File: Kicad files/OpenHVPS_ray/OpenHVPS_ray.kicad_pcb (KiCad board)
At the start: 2 copper layers, 45.8 x 20.6 mm, 69 parts, among them J1 Conn_01x03_Male, J2 Conn_01x03_Male, Q1 FQT7N10, Q2 BC846A, Q3 MMDT3906, U1 MAX6008AEUR+T, U2 74HC14, U3 MAX4162, U4 CD14538BM

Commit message: Added rays version
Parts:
- removed J1: Conn_01x03_Male, Connector_PinHeader_2.54mm:PinHeader_1x03_P2.54mm_Vertical
- removed JP1: 7317, Jumper:SolderJumper-2_P1.3mm_Open_RoundedPad1.0x1.5mm
- removed R2: 10M, Resistor_SMD:R_1206_3216Metric
- added REF**: PinHeader_1x01_P2.54mm_Vertical, Connector_PinHeader_2.54mm:PinHeader_1x01_P2.54mm_Vertical, F.Cu at (164.6, 75.7)
- added REF**: PinHeader_1x01_P2.54mm_Vertical, Connector_PinHeader_2.54mm:PinHeader_1x01_P2.54mm_Vertical, F.Cu at (125.2, 75.7)
- added REF**: PinHeader_1x01_P2.54mm_Vertical, Connector_PinHeader_2.54mm:PinHeader_1x01_P2.54mm_Vertical, F.Cu at (164.3, 59.4)
- added REF**: PinHeader_1x01_P2.54mm_Vertical, Connector_PinHeader_2.54mm:PinHeader_1x01_P2.54mm_Vertical, F.Cu at (125.2, 59.7)
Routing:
- net GND: track 118.9 -> 125.2 mm, vias 14 -> 13
- net Net-(H2-Pad1): track 7.99 -> 4.16 mm
- net +3V3: track 65.5 -> 63.2 mm
- net Net-(C21-Pad2): track 8.04 -> 5.94 mm
- net Net-(D2-Pad2): track 34.6 -> 32.5 mm
- net Net-(JP1-Pad1): track 1.70 -> 0.00 mm
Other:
- board size 45.8 x 20.6 mm -> 43.4 x 20.6 mm
- board text added: "SafePulse V0.9 (ray)"
- board text removed: "SafePulse V0.9"

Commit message: Added Ray version
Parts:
- removed the REF** at (164.6, 75.7)
- removed the REF** at (125.2, 75.7)
- removed the REF** at (125.2, 59.7)
- added ?: LOGO, Symbol:QR_code_SafePulse, F.Cu at (157.2, 66.3)
- added H2: Anode, TestPoint:TestPoint_Loop_D2.50mm_Drill1.85mm, F.Cu at (164.3, 72.4)
- added REF**: PinHeader_1x01_P2.54mm_Vertical, Connector_PinHeader_2.54mm:PinHeader_1x01_P2.54mm_Vertical, F.Cu at (164.3, 62.2)
- H1, H2: footprint TestPoint:TestPoint_Loop_D3.80mm_Drill2.0mm -> TestPoint:TestPoint_Loop_D2.50mm_Drill1.0mm
- moved H2 1.95 mm to (164.3, 68.8)
- moved R1 1.04 mm to (164.1, 65.5), turned to 0 degrees
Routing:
- net GND: track 125.2 -> 121.0 mm
- net Net-(H2-Pad1): track 4.16 -> 8.16 mm
- net Net-(C21-Pad2): track 5.94 -> 7.63 mm
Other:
- board size 43.4 x 20.6 mm -> 40.6 x 20.8 mm

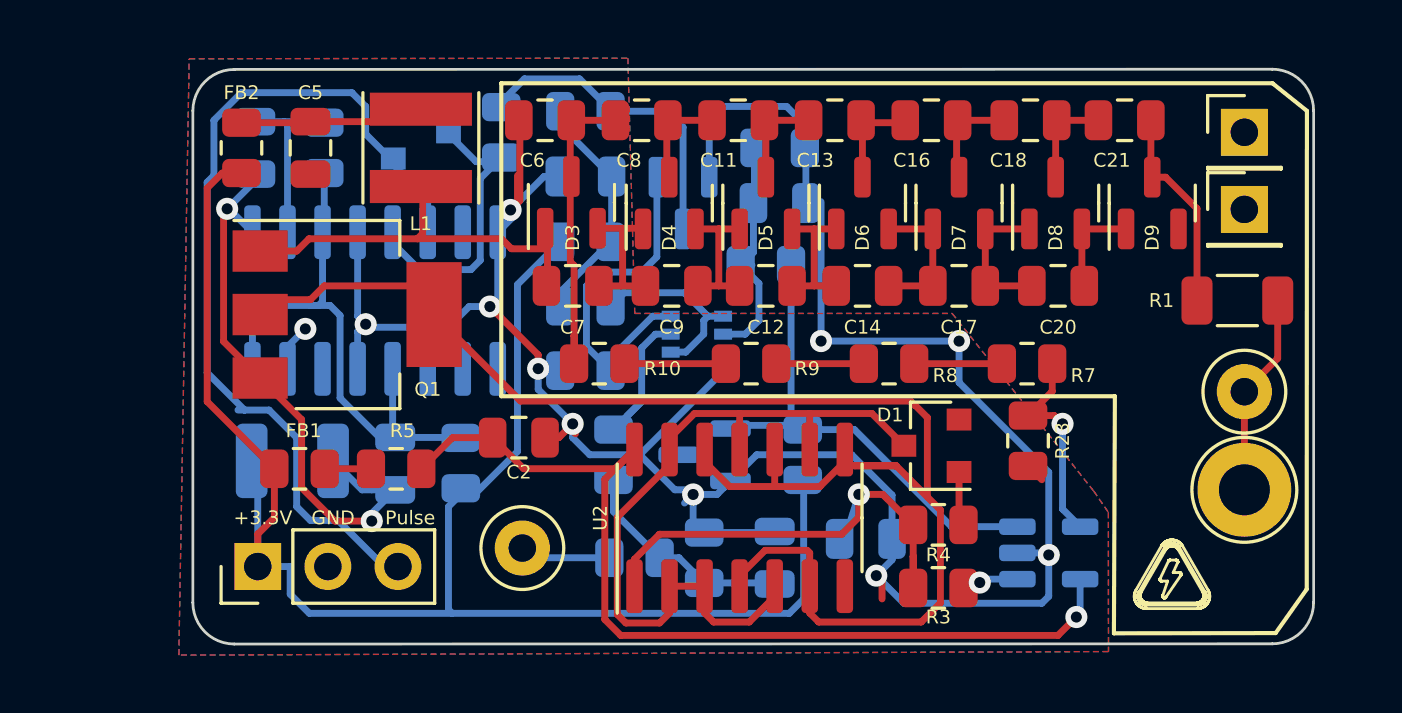
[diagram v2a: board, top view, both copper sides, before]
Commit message: Flipped R1 and +-P-GND and naming
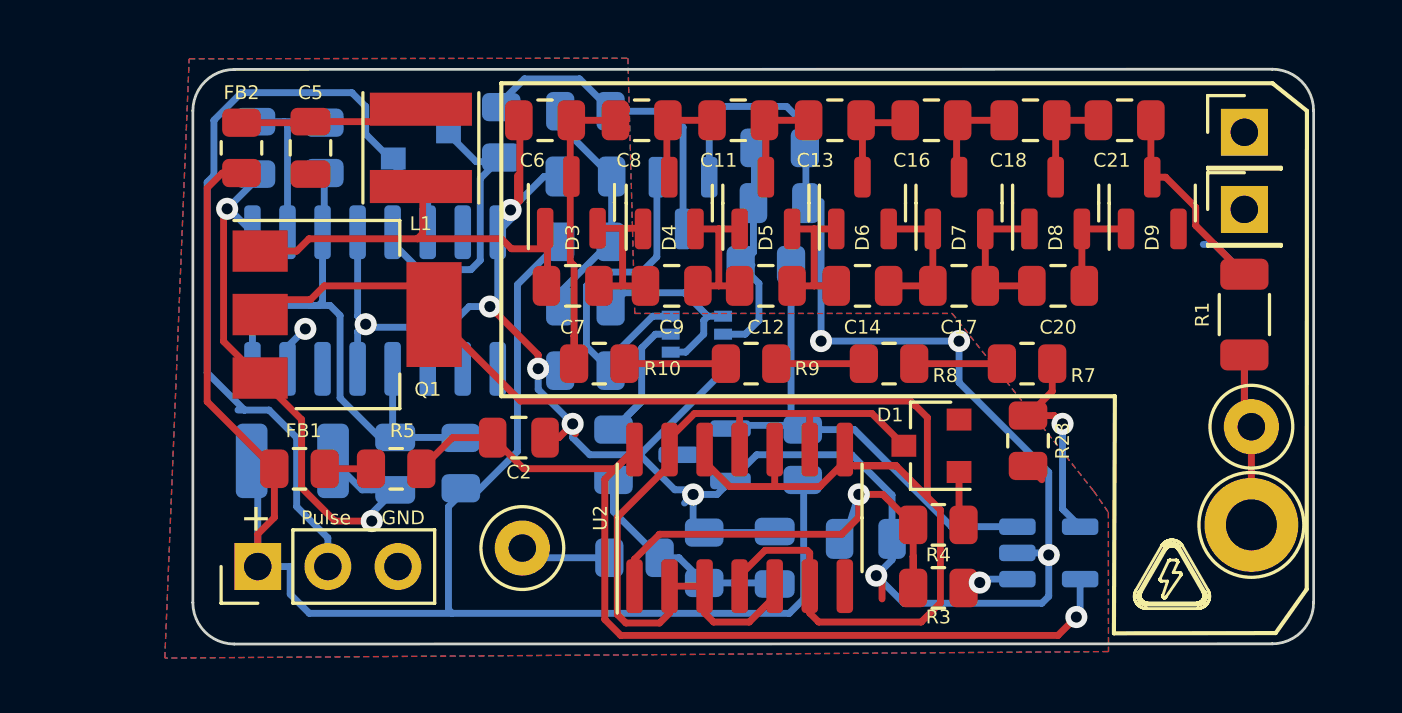
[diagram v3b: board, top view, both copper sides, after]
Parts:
- moved H2 1.30 mm to (164.6, 70.1)
- moved H2 1.30 mm to (164.6, 73.7)
- moved R1 0.57 mm to (164.3, 66.0), turned to -90 degrees
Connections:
- net Net-(D9-Pad2) renamed no_connect_(D9-Pad2)
- net Net-(U1-Pad3) renamed no_connect_(U1-Pad3)
- net Net-(U4-Pad10) renamed no_connect_(U4-Pad10)
- net Net-(U4-Pad14) renamed no_connect_(U4-Pad14)
- net Net-(U4-Pad7) renamed no_connect_(U4-Pad7)
- net Net-(U4-Pad9) renamed no_connect_(U4-Pad9)
- D2 pad 2: Net-(D2-Pad2) -> Net-(J1-Pad2)
- J2 pad 2: GND -> Net-(J1-Pad2)
- J2 pad 3: Net-(D2-Pad2) -> GND
- U4 pad 6: Net-(D2-Pad2) -> Net-(J1-Pad2)
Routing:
- net Net-(D2-Pad2): track 32.5 -> 0.00 mm
- net Net-(J1-Pad2): track 0.00 -> 30.6 mm
- net Net-(C21-Pad2): track 7.63 -> 9.32 mm
- net Net-(H2-Pad1): track 8.16 -> 8.97 mm
- net GND: track 121.0 -> 121.7 mm
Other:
- board text added: "+"
- board text added: "Safecast"
- board text removed: "+3.3V"
- board text removed: "SafePulse V0.9 (ray)"

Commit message: Made new branch
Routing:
- net Net-(H2-Pad1): track 8.97 -> 6.62 mm
- net Net-(C21-Pad2): track 9.32 -> 7.39 mm
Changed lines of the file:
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@@
     (property "Sheet name" "")
     (attr smd)
-    (fp_text reference "R1" (at 0 1.524 90) (layer "F.SilkS")
+    (fp_text reference "R1" (at 0 -1.524 90) (layer "F.SilkS")
       (effects (font (size 0.5 0.5) (thickness 0.075)))
     )
@@
   (segment (start 160.9123 59.0002) (end 161 59.0875) (width 0.25) (layer "F.Cu") (net 25))
   (segment (start 160.9125 59) (end 160.9123 59.0002) (width 0.25) (layer "F.Cu") (net 25))
-  (segment (start 162.85 63.496549) (end 163.257049 63.496549) (width 0.25) (layer "B.Cu") (net 25))
-  (segment (start 163.257049 63.496549) (end 164.338 64.5775) (width 0.25) (layer "B.Cu") (net 25))
   (segment (start 150.841553 69.624) (end 152.011553 70.794) (width 0.25) (layer "F.Cu") (net 26))
   (segment (start 144.414 69.624) (end 143.51 70.5278) (width 0.25) (layer "F.Cu") (net 26))
@@
   (segment (start 138.606 74.8515) (end 138.43 74.676) (width 0.25) (layer "B.Cu") (net 33))
   (segment (start 141.3275 74.8515) (end 138.5275 74.8515) (width 0.25) (layer "B.Cu") (net 33))
-  (segment (start 164.592 70.104) (end 164.592 73.66) (width 0.25) (layer "F.Cu") (net 34))
-  (segment (start 164.338 69.85) (end 164.592 70.104) (width 0.25) (layer "F.Cu") (net 34))
   (segment (start 164.338 67.5025) (end 164.338 69.85) (width 0.25) (layer "F.Cu") (net 34))
+  (segment (start 164.338 69.85) (end 164.592 70.104) (width 0.25) (layer "F.Cu") (net 34))
+  (segment (start 164.592 70.104) (end 164.592 73.66) (width 0.25) (layer "F.Cu") (net 34))
   (segment (start 164.338 69.85) (end 164.592 70.104) (width 0.25) (layer "B.Cu") (net 34))
-  (segment (start 164.338 67.5025) (end 164.338 69.85) (width 0.25) (layer "B.Cu") (net 34))
   (segment (start 146.55 62) (end 146.55 63.7875) (width 0.25) (layer "B.Cu") (net 35))
   (segment (start 146.5875 61.9625) (end 146.55 62) (width 0.25) (layer "B.Cu") (net 35))
